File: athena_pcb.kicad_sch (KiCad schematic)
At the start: 32 parts, among them J1 Conn_02x03_Odd_Even, SW1 SW_Push, SW2 SW_Push, U1 NRF5340-QKAA-R7, U2 BME280, Y1 32MHz, Y2 32.768kHz

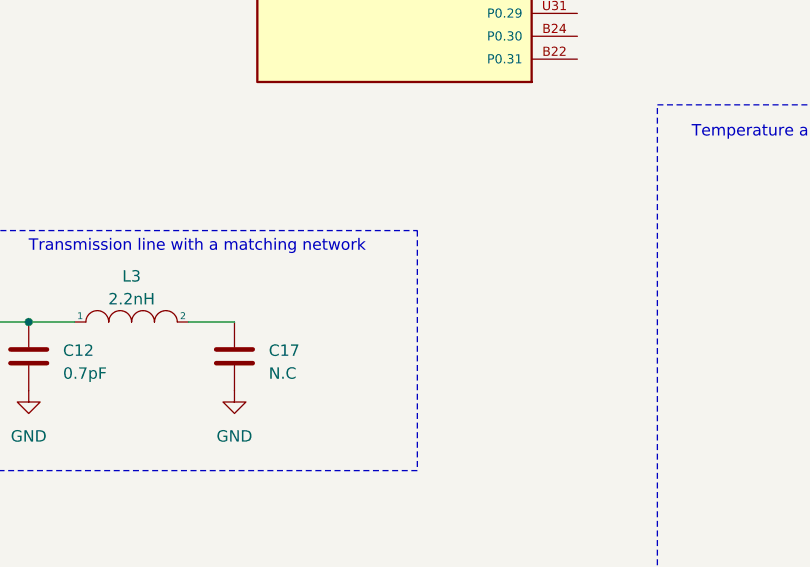
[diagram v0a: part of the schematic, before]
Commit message: Layout around NRF53 done
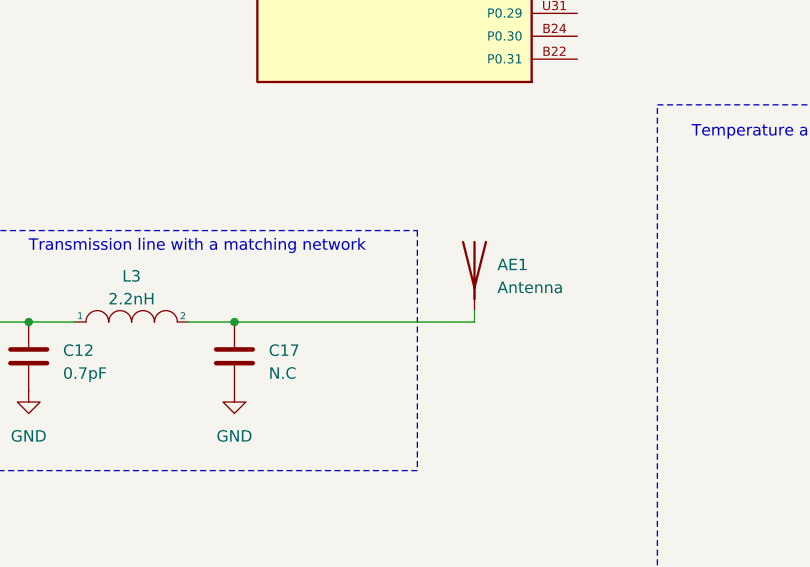
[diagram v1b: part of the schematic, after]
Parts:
- added AE1: Antenna, RF_Antenna:Texas_SWRA117D_2.4GHz_Left, symbol Device:Antenna
- C9: footprint Capacitor_SMD:C_0402_1005Metric -> Capacitor_SMD:C_0201_0603Metric
- L1, L2: footprint Inductor_SMD:L_0201_0603Metric -> Inductor_SMD:L_0603_1608Metric
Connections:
- net at C17.1, L3.2: now also AE1.1 (A)
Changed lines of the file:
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@@
   (junction (at 60.96 45.72) (diameter 0) (color 0 0 0 0)
+  )
+  (junction (at 162.56 128.27) (diameter 0) (color 0 0 0 0)
   )
   (junction (at 116.84 19.05) (diameter 0) (color 0 0 0 0)
@@
     (stroke (width 0) (type default))
   )
+  (wire (pts (xy 189.23 127) (xy 189.23 128.27))
+    (stroke (width 0) (type default))
+  )
   (wire (pts (xy 111.76 27.94) (xy 111.76 35.56))
     (stroke (width 0) (type default))
@@
   )
   (wire (pts (xy 139.7 128.27) (xy 144.78 128.27))
+    (stroke (width 0) (type default))
+  )
+  (wire (pts (xy 162.56 128.27) (xy 189.23 128.27))
     (stroke (width 0) (type default))
   )
@@
       (effects (font (size 1.27 1.27)))
     )
-    (property "Footprint" "Inductor_SMD:L_0201_0603Metric" (at 67.31 43.18 0)
+    (property "Footprint" "Inductor_SMD:L_0603_1608Metric" (at 67.31 43.18 0)
       (effects (font (size 1.27 1.27)) hide)
     )
@@
       (effects (font (size 1.27 1.27)) (justify left))
     )
-    (property "Footprint" "Capacitor_SMD:C_0402_1005Metric" (at 119.0752 43.18 0)
+    (property "Footprint" "Capacitor_SMD:C_0201_0603Metric" (at 119.0752 43.18 0)
       (effects (font (size 1.27 1.27)) hide)
     )
@@
     )
   )
+  (symbol (lib_id "Device:Antenna") (at 189.23 121.92 0) (unit 1)
+    (in_bom yes) (on_board yes) (dnp no) (fields_autoplaced)
+    (property "Reference" "AE1" (at 191.77 121.92 0)
+      (effects (font (size 1.27 1.27)) (justify left))
+    )
+    (property "Value" "Antenna" (at 191.77 124.46 0)
+      (effects (font (size 1.27 1.27)) (justify left))
+    )
+    (property "Footprint" "RF_Antenna:Texas_SWRA117D_2.4GHz_Left" (at 189.23 121.92 0)
+      (effects (font (size 1.27 1.27)) hide)
+    )
+    (property "Datasheet" "~" (at 189.23 121.92 0)
+      (effects (font (size 1.27 1.27)) hide)
+    )
+    (pin "1")
+    (instances
+      (project "athena_pcb"
+        (path "/fadb6411-1081-41a3-ba72-837bcce93ee0"
+          (reference "AE1") (unit 1)
+        )
+      )
+    )
+  )
   (symbol (lib_id "Device:C") (at 257.81 119.38 90) (unit 1)
     (in_bom yes) (on_board yes) (dnp no)
@@
       (effects (font (size 1.27 1.27)))
     )
-    (property "Footprint" "Inductor_SMD:L_0201_0603Metric" (at 36.83 30.48 0)
-      (effects (font (size 1.27 1.27)) hide)
-    )
+    (property "Footprint" "Inductor_SMD:L_0603_1608Metric" (at 36.83 30.48 0)
+      (effects (font (size 1.27 1.27)) hide)
+    )

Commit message: Added new 0201 capacitor footprint
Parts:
- C3: footprint Capacitor_SMD:C_0201_0603Metric -> GRM033R71C301JA01D:CAPC0603X33N
- U1: footprint XCVR_NRF5340-QKAA-R7 -> NRF5340-QKAA-R7:XCVR_NRF5340-QKAA-R7
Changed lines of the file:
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@@
       (effects (font (size 1.27 1.27)))
     )
-    (property "Footprint" "XCVR_NRF5340-QKAA-R7" (at 93.98 48.26 0)
+    (property "Footprint" "NRF5340-QKAA-R7:XCVR_NRF5340-QKAA-R7" (at 93.98 48.26 0)
       (effects (font (size 1.27 1.27)) (justify bottom) hide)
     )
@@
       (effects (font (size 1.27 1.27)) (justify left))
     )
-    (property "Footprint" "XCVR_NRF5340-QKAA-R7" (at 180.34 58.42 0)
+    (property "Footprint" "NRF5340-QKAA-R7:XCVR_NRF5340-QKAA-R7" (at 180.34 58.42 0)
       (effects (font (size 1.27 1.27)) (justify bottom) hide)
     )
@@
       (effects (font (size 1.27 1.27)) (justify left))
     )
-    (property "Footprint" "Capacitor_SMD:C_0201_0603Metric" (at 41.6052 43.18 0)
+    (property "Footprint" "GRM033R71C301JA01D:CAPC0603X33N" (at 41.6052 43.18 0)
       (effects (font (size 1.27 1.27)) hide)
     )
@@
       (effects (font (size 1.27 1.27)))
     )
-    (property "Footprint" "XCVR_NRF5340-QKAA-R7" (at 254 49.53 0)
+    (property "Footprint" "NRF5340-QKAA-R7:XCVR_NRF5340-QKAA-R7" (at 254 49.53 0)
       (effects (font (size 1.27 1.27)) (justify bottom) hide)
     )
@@
       (effects (font (size 1.27 1.27)))
     )
-    (property "Footprint" "XCVR_NRF5340-QKAA-R7" (at 100.33 135.89 0)
+    (property "Footprint" "NRF5340-QKAA-R7:XCVR_NRF5340-QKAA-R7" (at 100.33 135.89 0)
       (effects (font (size 1.27 1.27)) (justify bottom) hide)
     )

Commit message: Added board outline
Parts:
- C10, C11, C12, C13, C14, C15, C16, C17, C18, C19, C6, C8, C9: footprint Capacitor_SMD:C_0201_0603Metric -> GRM033R71C301JA01D:CAPC0603X33N
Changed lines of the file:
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@@
       (effects (font (size 1.27 1.27)) (justify left))
     )
-    (property "Footprint" "Capacitor_SMD:C_0201_0603Metric" (at 127.9652 26.67 0)
+    (property "Footprint" "GRM033R71C301JA01D:CAPC0603X33N" (at 127.9652 26.67 0)
       (effects (font (size 1.27 1.27)) hide)
     )
@@
       (effects (font (size 1.27 1.27)) (justify left))
     )
-    (property "Footprint" "Capacitor_SMD:C_0201_0603Metric" (at 140.6652 135.89 0)
+    (property "Footprint" "GRM033R71C301JA01D:CAPC0603X33N" (at 140.6652 135.89 0)
       (effects (font (size 1.27 1.27)) hide)
     )
@@
       (effects (font (size 1.27 1.27)) (justify left))
     )
-    (property "Footprint" "Capacitor_SMD:C_0201_0603Metric" (at 129.2352 43.18 0)
+    (property "Footprint" "GRM033R71C301JA01D:CAPC0603X33N" (at 129.2352 43.18 0)
       (effects (font (size 1.27 1.27)) hide)
     )
@@
       (effects (font (size 1.27 1.27)) (justify left))
     )
-    (property "Footprint" "Capacitor_SMD:C_0201_0603Metric" (at 149.5552 43.18 0)
+    (property "Footprint" "GRM033R71C301JA01D:CAPC0603X33N" (at 149.5552 43.18 0)
       (effects (font (size 1.27 1.27)) hide)
     )
@@
       (effects (font (size 1.27 1.27)) (justify left))
     )
-    (property "Footprint" "Capacitor_SMD:C_0201_0603Metric" (at 139.3952 43.18 0)
+    (property "Footprint" "GRM033R71C301JA01D:CAPC0603X33N" (at 139.3952 43.18 0)
       (effects (font (size 1.27 1.27)) hide)
     )
@@
       (effects (font (size 1.27 1.27)) (justify left))
     )
-    (property "Footprint" "Capacitor_SMD:C_0201_0603Metric" (at 119.0752 43.18 0)
+    (property "Footprint" "GRM033R71C301JA01D:CAPC0603X33N" (at 119.0752 43.18 0)
       (effects (font (size 1.27 1.27)) hide)
     )
@@
       (effects (font (size 1.27 1.27)) (justify left))
     )
-    (property "Footprint" "Capacitor_SMD:C_0201_0603Metric" (at 61.9252 77.47 0)
+    (property "Footprint" "GRM033R71C301JA01D:CAPC0603X33N" (at 61.9252 77.47 0)
       (effects (font (size 1.27 1.27)) hide)
     )
@@
       (effects (font (size 1.27 1.27)) (justify left))
     )
-    (property "Footprint" "Capacitor_SMD:C_0201_0603Metric" (at 138.1252 26.67 0)
+    (property "Footprint" "GRM033R71C301JA01D:CAPC0603X33N" (at 138.1252 26.67 0)
       (effects (font (size 1.27 1.27)) hide)
     )
@@
       (effects (font (size 1.27 1.27)) (justify left))
     )
-    (property "Footprint" "Capacitor_SMD:C_0201_0603Metric" (at 117.8052 26.67 0)
+    (property "Footprint" "GRM033R71C301JA01D:CAPC0603X33N" (at 117.8052 26.67 0)
       (effects (font (size 1.27 1.27)) hide)
     )
@@
       (effects (font (size 1.27 1.27)))
     )
-    (property "Footprint" "Capacitor_SMD:C_0201_0603Metric" (at 246.38 118.4148 0)
+    (property "Footprint" "GRM033R71C301JA01D:CAPC0603X33N" (at 246.38 118.4148 0)
       (effects (font (size 1.27 1.27)) hide)
     )
@@
       (effects (font (size 1.27 1.27)))
     )
-    (property "Footprint" "Capacitor_SMD:C_0201_0603Metric" (at 261.62 118.4148 0)
+    (property "Footprint" "GRM033R71C301JA01D:CAPC0603X33N" (at 261.62 118.4148 0)
       (effects (font (size 1.27 1.27)) hide)
     )
@@
       (effects (font (size 1.27 1.27)) (justify left))
     )
-    (property "Footprint" "Capacitor_SMD:C_0201_0603Metric" (at 148.2852 26.67 0)
+    (property "Footprint" "GRM033R71C301JA01D:CAPC0603X33N" (at 148.2852 26.67 0)
       (effects (font (size 1.27 1.27)) hide)
     )
@@
       (effects (font (size 1.27 1.27)) (justify left))
     )
-    (property "Footprint" "Capacitor_SMD:C_0201_0603Metric" (at 163.5252 135.89 0)
-      (effects (font (size 1.27 1.27)) hide)
-    )
+    (property "Footprint" "GRM033R71C301JA01D:CAPC0603X33N" (at 163.5252 135.89 0)
+      (effects (font (size 1.27 1.27)) hide)
+    )

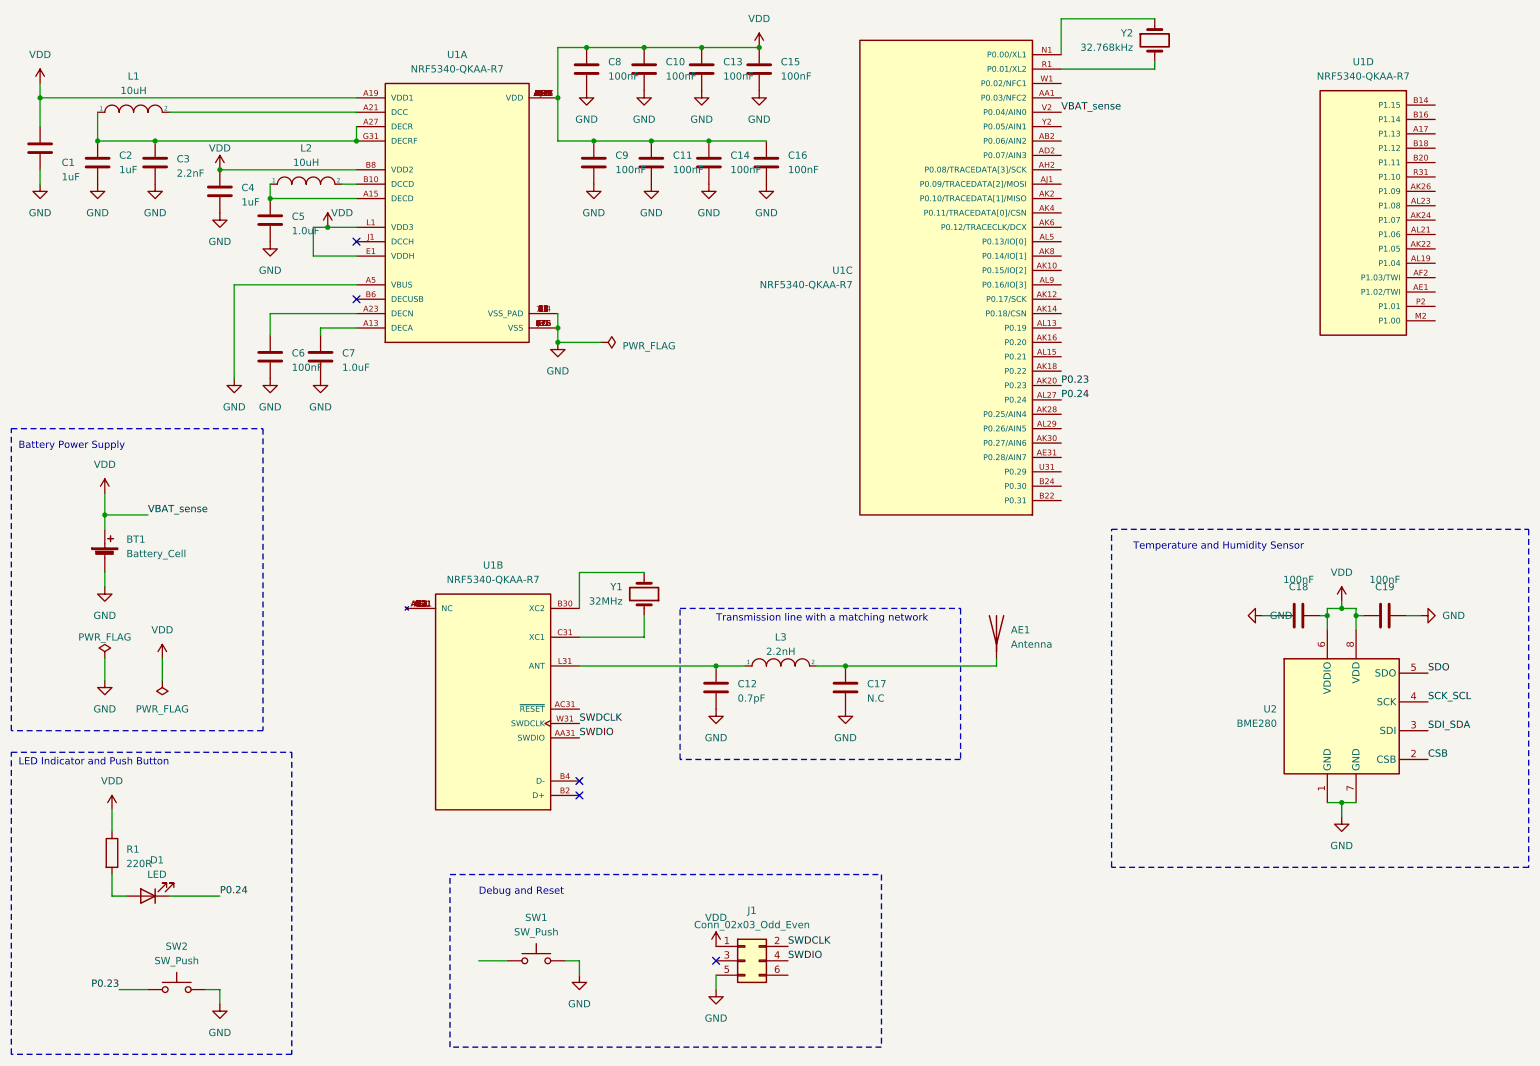
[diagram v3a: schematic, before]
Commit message: Added testpoints
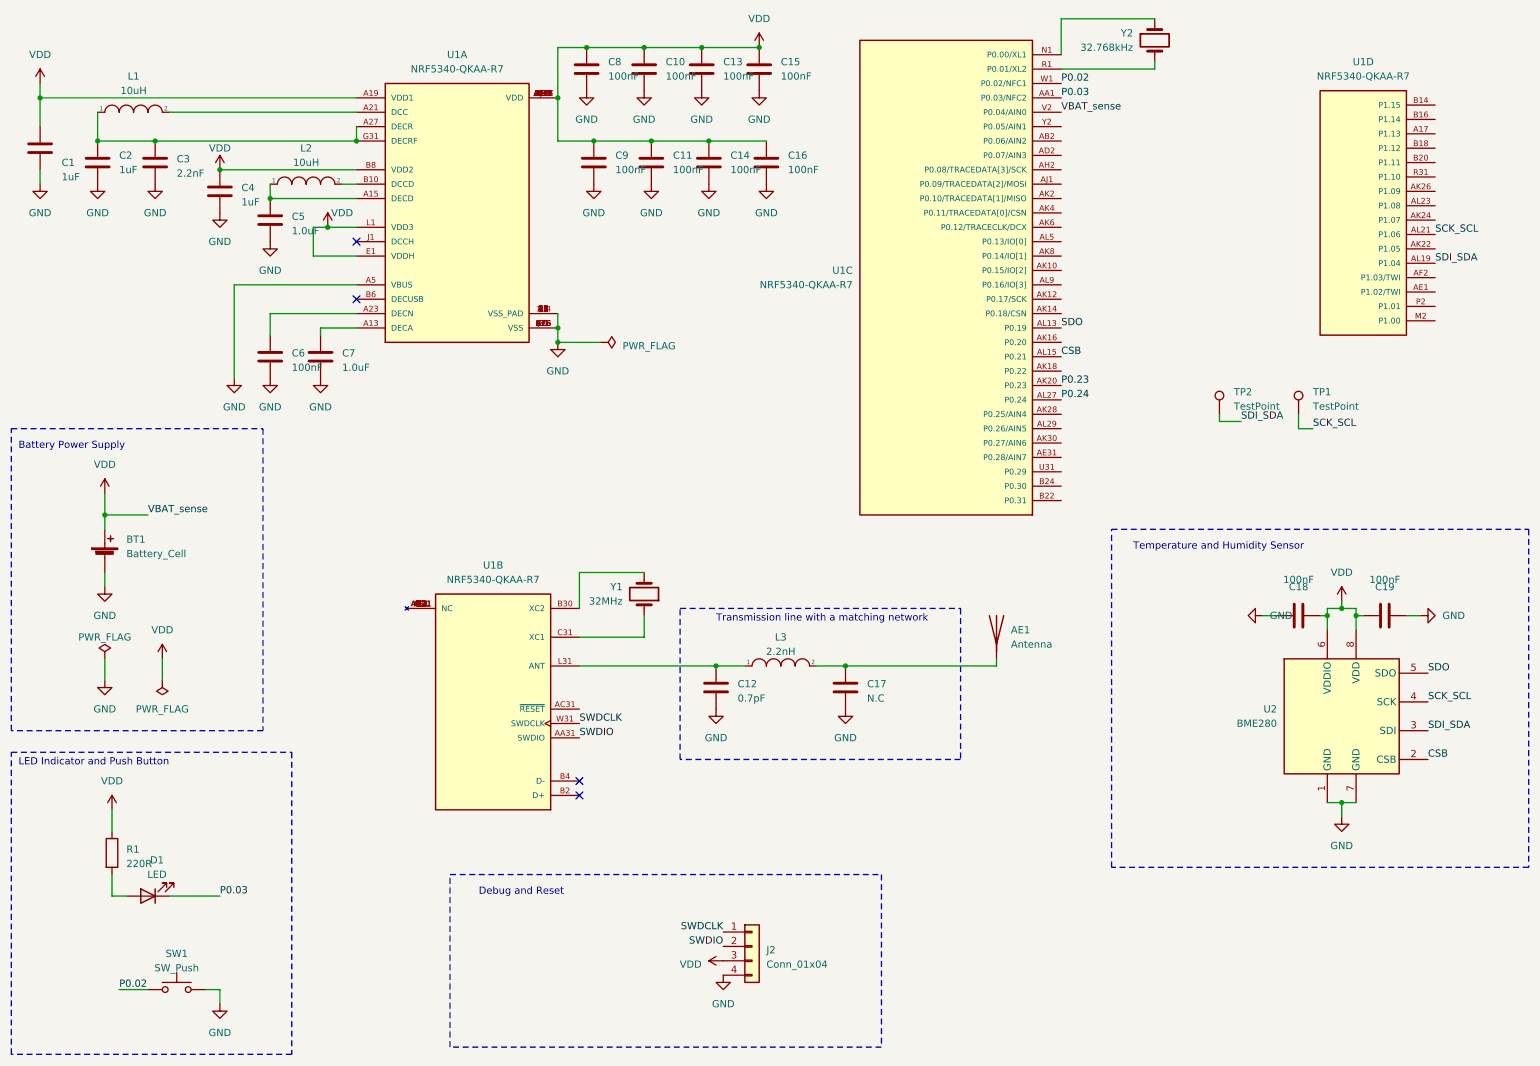
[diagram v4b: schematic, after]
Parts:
- removed J1: Conn_02x03_Odd_Even, Connector_PinHeader_1.27mm:PinHeader_2x03_P1.27mm_Vertical, symbol Connector_Generic:Conn_02x03_Odd_Even
- removed SW1: SW_Push, Button_Switch_SMD:SW_Push_SPST_NO_Alps_SKRK, symbol Switch:SW_Push
- added J2: Conn_01x04, Connector_PinSocket_1.27mm:PinSocket_1x04_P1.27mm_Vertical, symbol Connector_Generic:Conn_01x04
- added TP1, TP2: TestPoint, TestPoint:TestPoint_Pad_D1.0mm, symbol Connector:TestPoint
- renumbered SW2 to SW1
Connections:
- net CSB: now also U1.AL15 (P0.21)
- net GND: now also J2.4 (Pin_4)
- net P0.23: no longer SW1.1
- net P0.24: no longer D1.1 (K)
- net SCK_SCL: now also U1.AL21 (P1.06), TP1.1
- net SDI_SDA: now also U1.AL19 (P1.04), TP2.1
- net SDO: now also U1.AL13 (P0.19)
- net SWDCLK: now also J2.1 (Pin_1)
- net SWDIO: now also J2.2 (Pin_2)
- net VDD: now also J2.3 (Pin_3)
- net P0.03: now reaches U1.AA1 (P0.03/NFC2)
- net P0.03: now also D1.1 (K)
- net P0.02: now reaches U1.W1 (P0.02/NFC1)
- net P0.02: now also SW1.1
- no-connect marks 5 -> 4
